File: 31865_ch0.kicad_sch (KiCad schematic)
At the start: 24 parts, among them CN1 WJ15EDGRM-3.81-4P-14-00A, SW1 MST22D18G2, T1 VPT87BB-01B, U1 MAX31865xTP, U2 VPS8504B, U3 TPS7A2033PDBVR, U4 TPS7A2033PDBVR, U5 ISO7741DWR

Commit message: complete schematic layout
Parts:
- added R: 47k, symbol Device:R
- added U: SN74LVC1G125DBVR, rtd-transmitter-library:SOT-23-5_L3.0-W1.7-P0.95-LS2.8-BL, symbol rtd-transmitter-library:SN74LVC1G125DBVR
- renumbered C10 to C, C11 to C, CN1 to CN, R3 to R, SW1 to SW
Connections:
- net GND1 is gone; now on net GND: U5.2 (GND1)
- net +5V: now also U.5 (VCC)
- net CH_SDO: now also U.4 (Y); no longer U5.6 (OUTD)
- net CH_~{CS}: now also U.1 (~{OE})
- net GND: now also U.3 (GND); no longer U5.15 (GND2)
- net local_gnd: now also U5.15 (GND2), R.2
- net SCLK: no longer names the net of U1.12 (SCLK), U5.13 (OUTB)
- net SDI: no longer names the net of U1.11 (SDI), U5.14 (OUTA)
- net SDO: no longer names the net of U1.14 (SDO), U5.11 (IND)
- net SDO: now also R.1
- net ~{CS}: no longer names the net of U1.13 (~{CS}), U5.12 (OUTC)
- new net CH_SDO_LOWZ: U.2 (A), U5.6 (OUTD)
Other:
- moved on the sheet: C, C1, C2, C3, C4, C5, C6, C7, C8, C9, CN, D1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

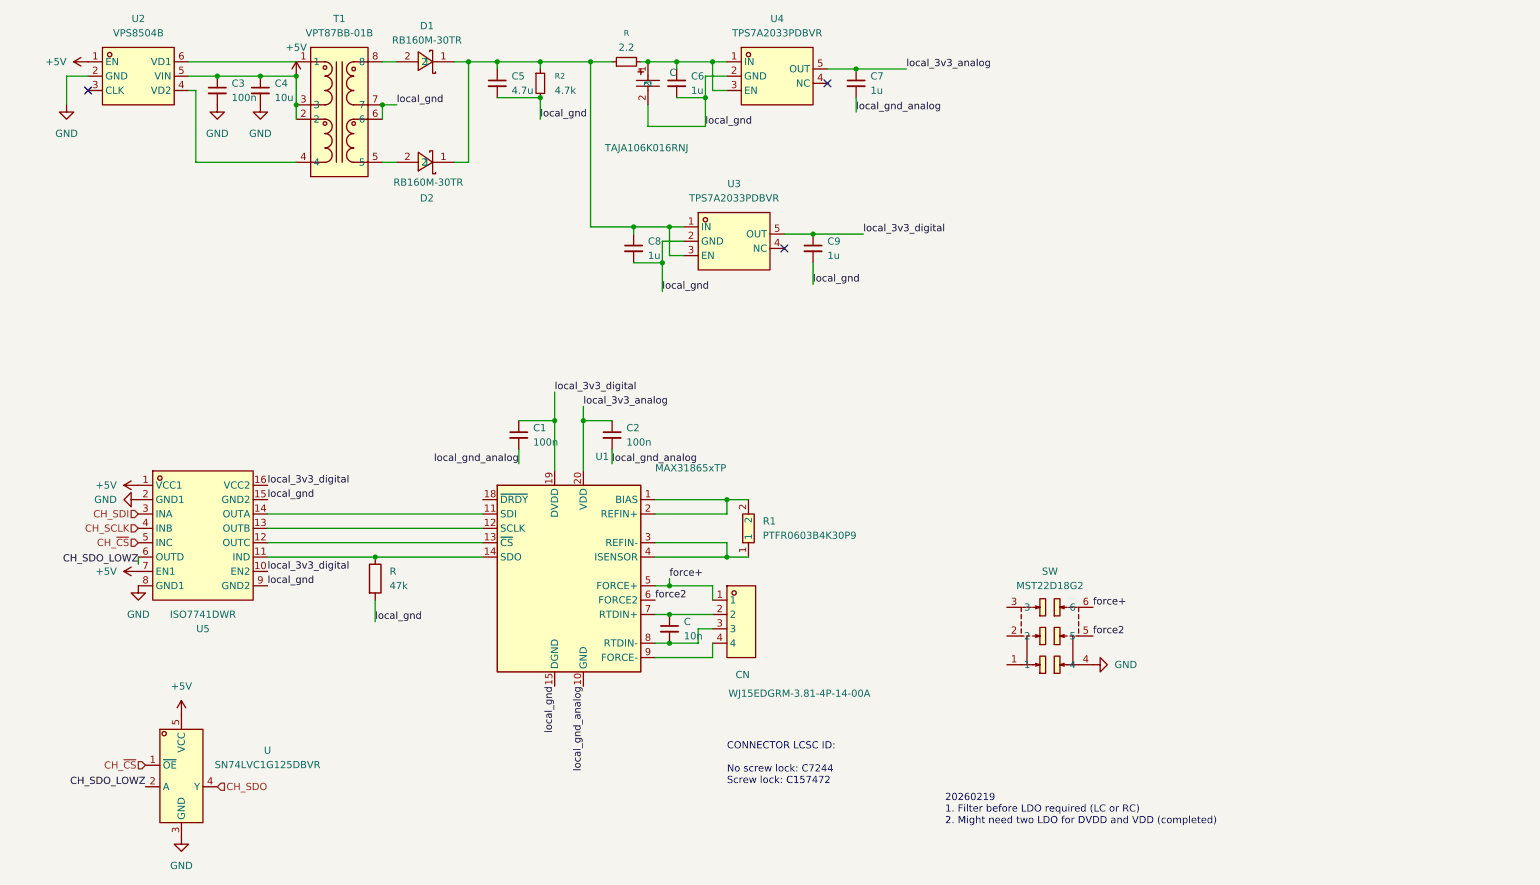
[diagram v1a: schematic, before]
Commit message: complete component alignment
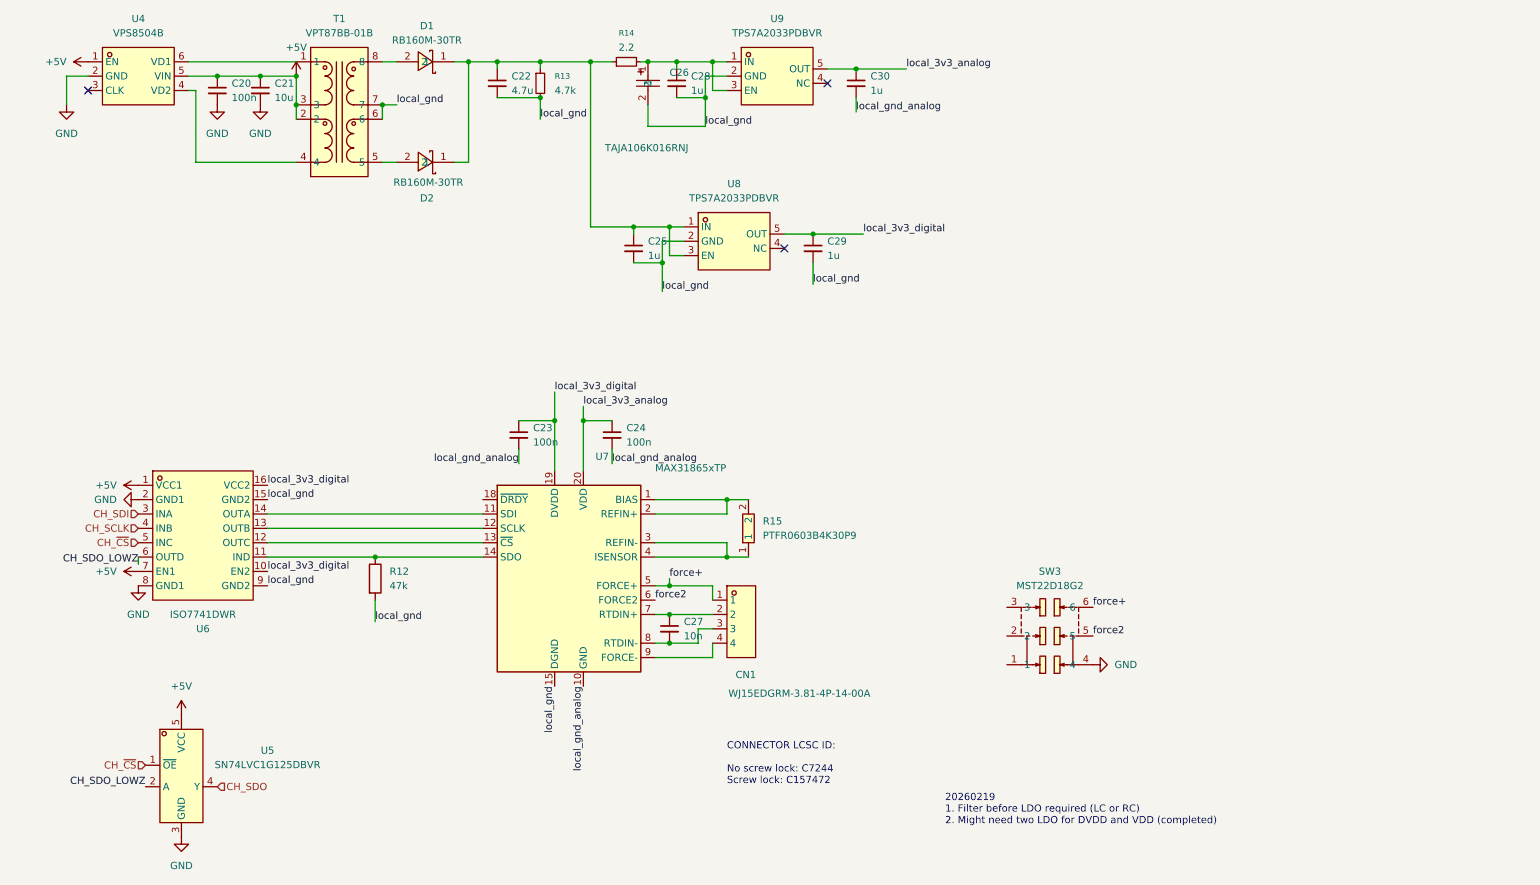
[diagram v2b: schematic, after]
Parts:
- C20: renamed from C3; footprint (none) -> Capacitor_SMD:C_0603_1608Metric
- C21: renamed from C4; footprint (none) -> Capacitor_SMD:C_0603_1608Metric
- C22: renamed from C5; footprint (none) -> Capacitor_SMD:C_0603_1608Metric
- C23: renamed from C1; footprint (none) -> Capacitor_SMD:C_0603_1608Metric
- C24: renamed from C2; footprint (none) -> Capacitor_SMD:C_0603_1608Metric
- C25: renamed from C8; footprint (none) -> Capacitor_SMD:C_0603_1608Metric
- C27: renamed from C; footprint (none) -> Capacitor_SMD:C_0603_1608Metric
- C28: renamed from C6; footprint (none) -> Capacitor_SMD:C_0603_1608Metric
- C29: renamed from C9; footprint (none) -> Capacitor_SMD:C_0603_1608Metric
- C30: renamed from C7; footprint (none) -> Capacitor_SMD:C_0603_1608Metric
- R12, R14: renamed from R; footprint (none) -> Resistor_SMD:R_0603_1608Metric
- R13: renamed from R2; footprint (none) -> Resistor_SMD:R_0603_1608Metric
- renumbered C to C26, CN to CN1, R1 to R15, SW to SW3, U2 to U4, U to U5, U5 to U6, U1 to U7, U3 to U8, U4 to U9

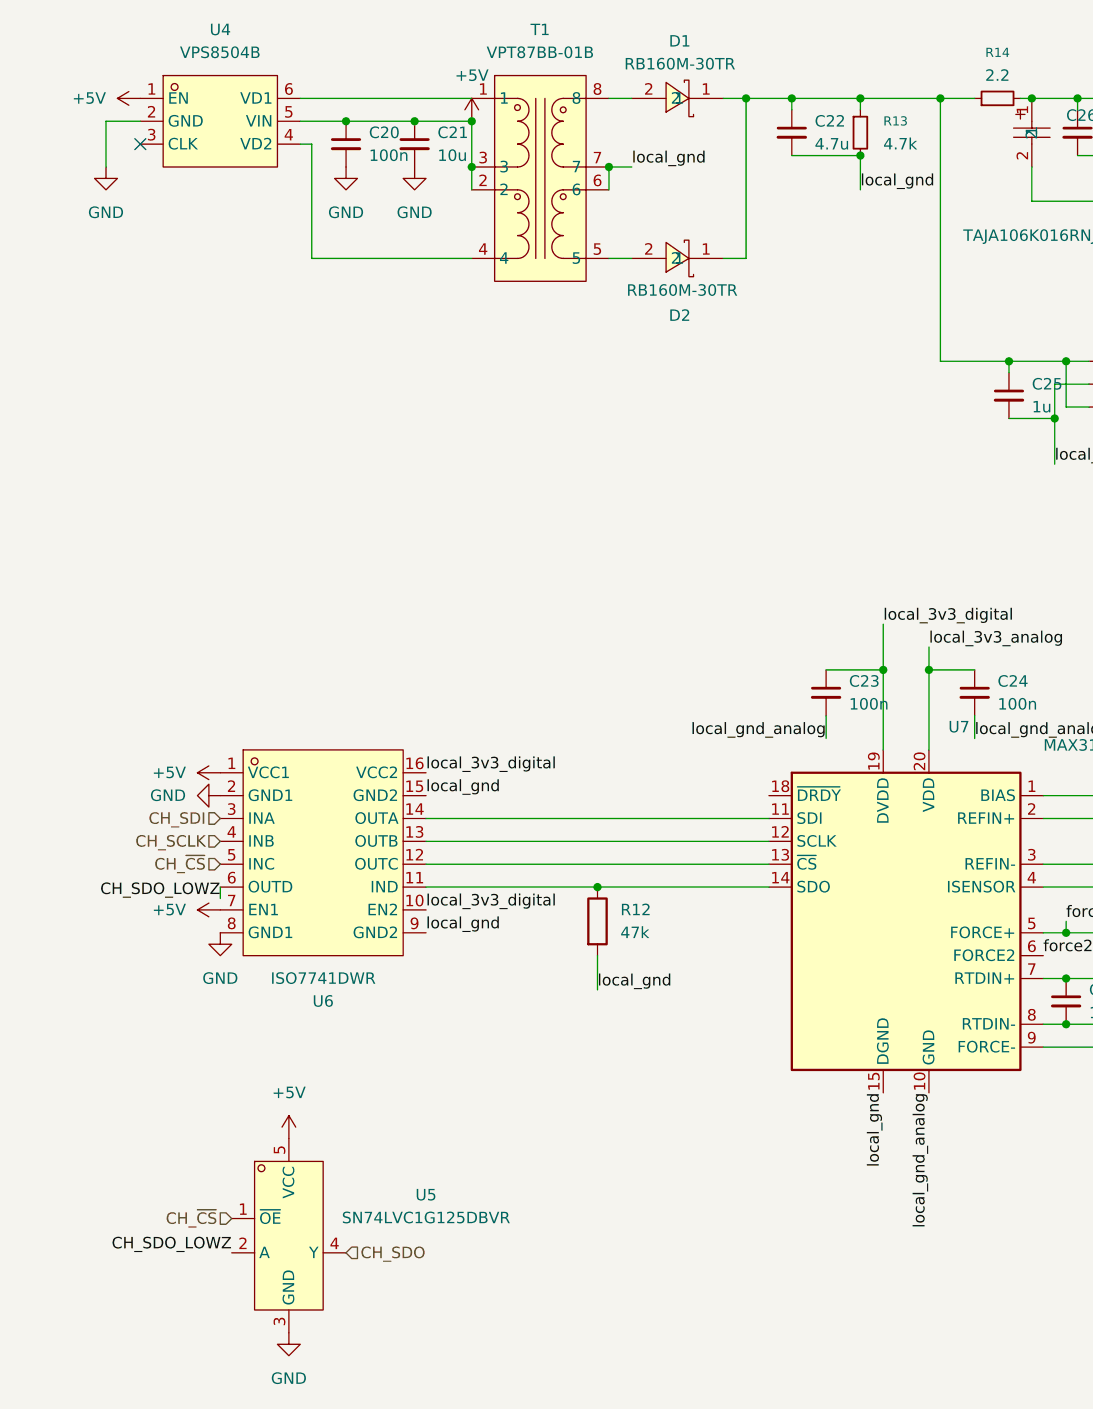
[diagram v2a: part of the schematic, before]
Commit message: start pcb layout, add sd card and screen
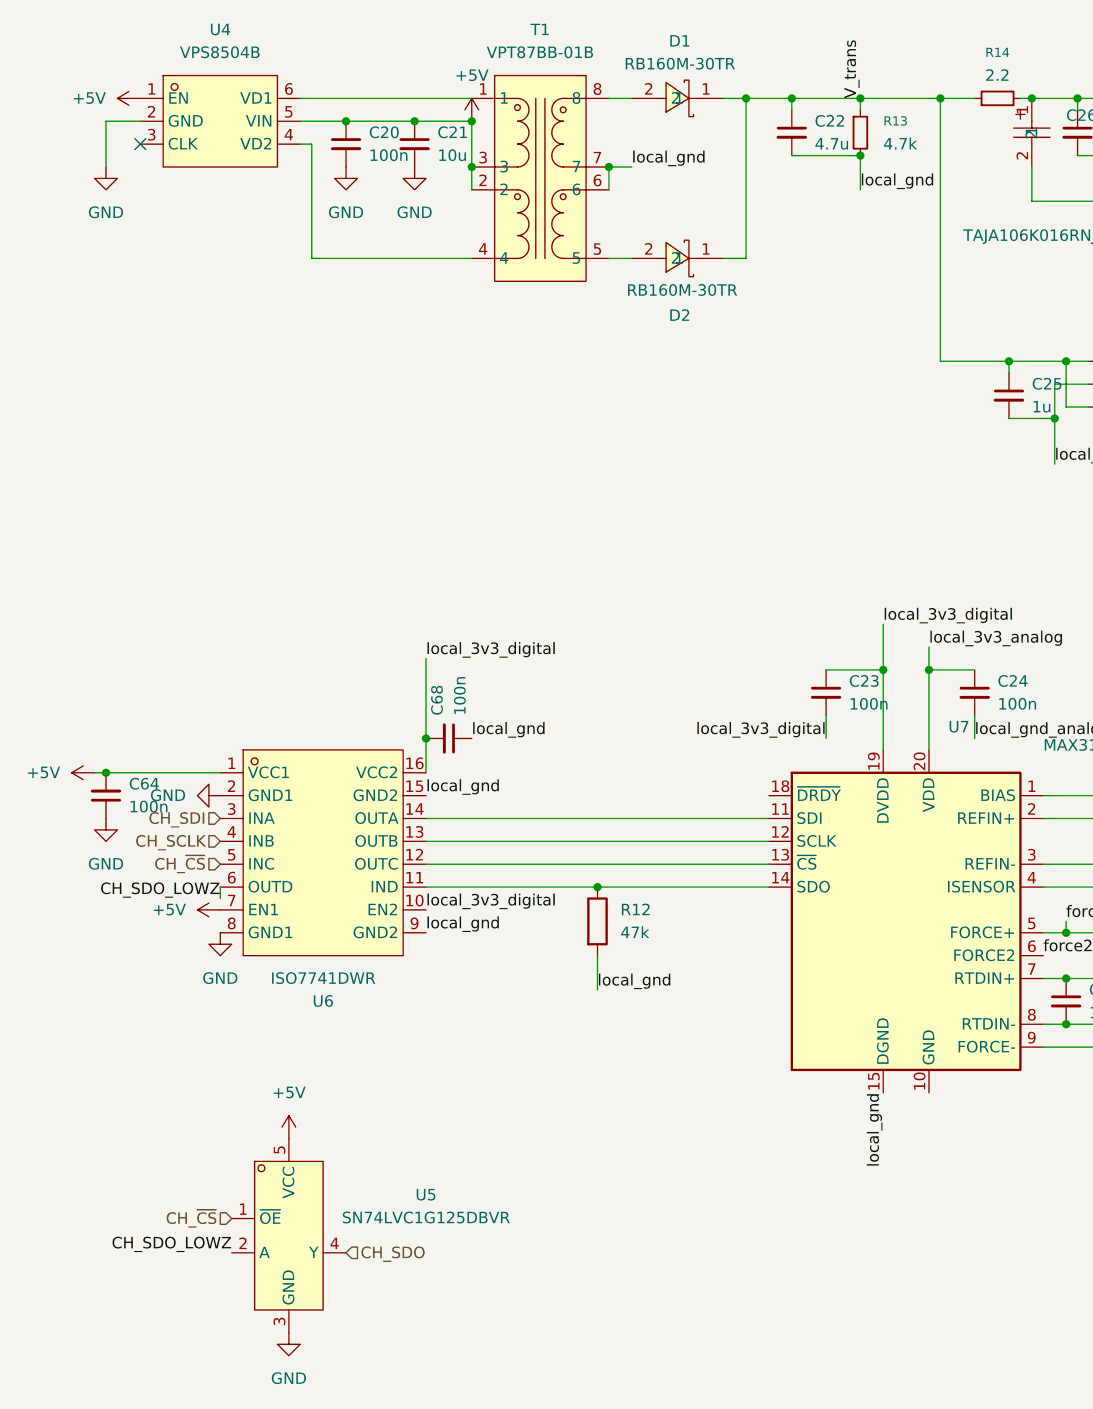
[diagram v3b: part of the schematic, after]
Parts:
- added C64, C68: 100n, Capacitor_SMD:C_0603_1608Metric, symbol Device:C_Small
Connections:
- net +5V: now also C64.2
- net GND: now also C64.1
- net local_3v3_digital: now also C23.2, C68.2
- net local_gnd: now also C68.1
- net local_gnd_analog: no longer C23.2, U7.10 (GND), U7.16 (GND), U7.21 (GND)
- net V_trans: now reaches C22.1, C25.1, D1.1, D2.1, R13.1, R14.1, U8.1 (IN), U8.3 (EN)
- new net: U7.10 (GND), U7.16 (GND), U7.21 (GND)

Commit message: Complete single channel design
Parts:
- removed CN1: WJ15EDGRM-3.81-4P-14-00A, rtd-transmitter-library:CONN-TH_4P-P3.81_WJ15EDGRM-3.81-04P-14-00A, symbol rtd-transmitter-library:WJ15EDGRM-3.81-4P-14-00A
- added CN5: WJ15EDGRC-3.81-4P, rtd-transmitter-library:CONN-TH_WJ15EDGRC-3.81-4P, symbol rtd-transmitter-library:WJ15EDGRC-3.81-4P
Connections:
- net GND: no longer SW3.4
- net force+: now also SW3.3, CN5.1; no longer SW3.6
- net force2: now also SW3.2; no longer SW3.5
- net local_gnd: now also C30.2
- net local_gnd_analog: now also SW3.1, U7.10 (GND), U7.16 (GND), U7.21 (GND); no longer C30.2
- net at C27.1, U7.7 (RTDIN+): now also CN5.2
- net at C27.2, U7.8 (RTDIN-): now also CN5.3
- net at U7.9 (FORCE-): now also CN5.4
- no-connect marks 3 -> 7
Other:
- note added: "20260219 1. Filter before LDO required (LC or RC) 2. Might need two LDO for DVDD and VDD (completed) 20260312 1. need to check TPS7A2033 voltage limitation"
- note removed: "20260219 1. Filter before LDO required (LC or RC) 2. Might need two LDO for DVDD and VDD (completed)"
